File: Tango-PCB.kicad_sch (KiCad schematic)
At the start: 60 parts, among them J1 PMOD, J10 Screw_Terminal_01x03, J11 Screw_Terminal_01x03, J12 Screw_Terminal_01x03, J13 Screw_Terminal_01x03, J14 Screw_Terminal_01x03, J15 Screw_Terminal_01x03, J16 Screw_Terminal_01x03, J17 Screw_Terminal_01x03, J18 Screw_Terminal_01x03, J19 Screw_Terminal_01x03, J2 EXT, J20 Screw_Terminal_01x03, J21 Screw_Terminal_01x03, J22 PWR, J23 SENSPWR, J26 PMOD, J3 Screw_Terminal_01x04, J4 Screw_Terminal_01x04, J5 Screw_Terminal_01x04, J6 Screw_Terminal_01x04, J7 Screw_Terminal_01x04, J8 Screw_Terminal_01x04, J9 Screw_Terminal_01x03, U1 ULN2803A, U2 ULN2803A, U3 ULN2803A

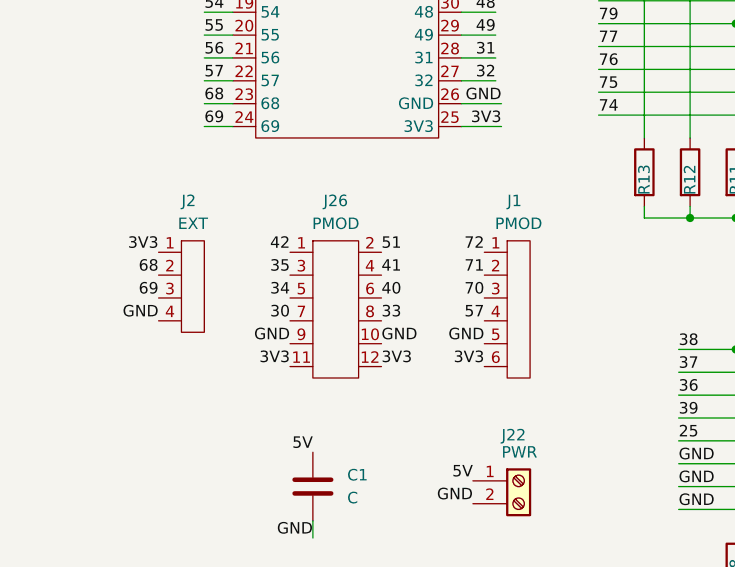
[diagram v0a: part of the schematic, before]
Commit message: Add SPI connector
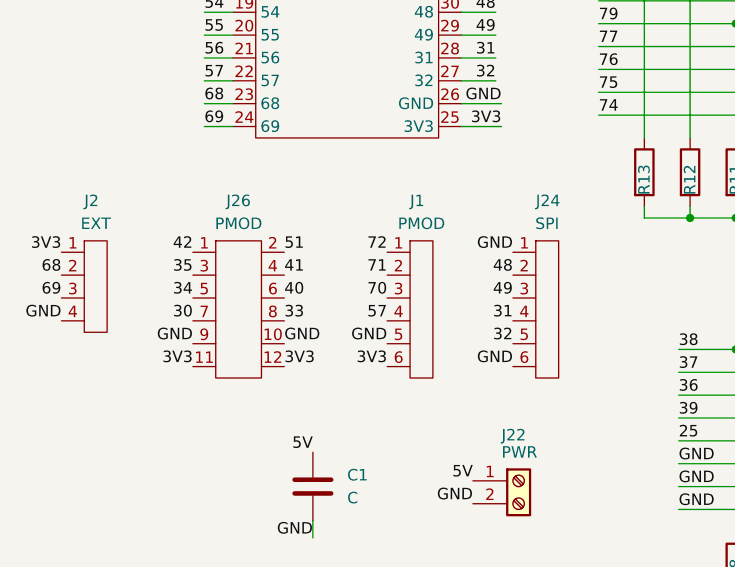
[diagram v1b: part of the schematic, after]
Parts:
- added J24: SPI, Connector_JST:JST_XH_S6B-XH-A-1_1x06_P2.50mm_Horizontal, symbol Library:Conn)01x06_pin
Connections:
- net 31: now also J24.4
- net 32: now also J24.5
- net 48: now also J24.2
- net 49: now also J24.3
- net GND: now also J24.1, J24.6
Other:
- moved on the sheet: J1, J2, J26

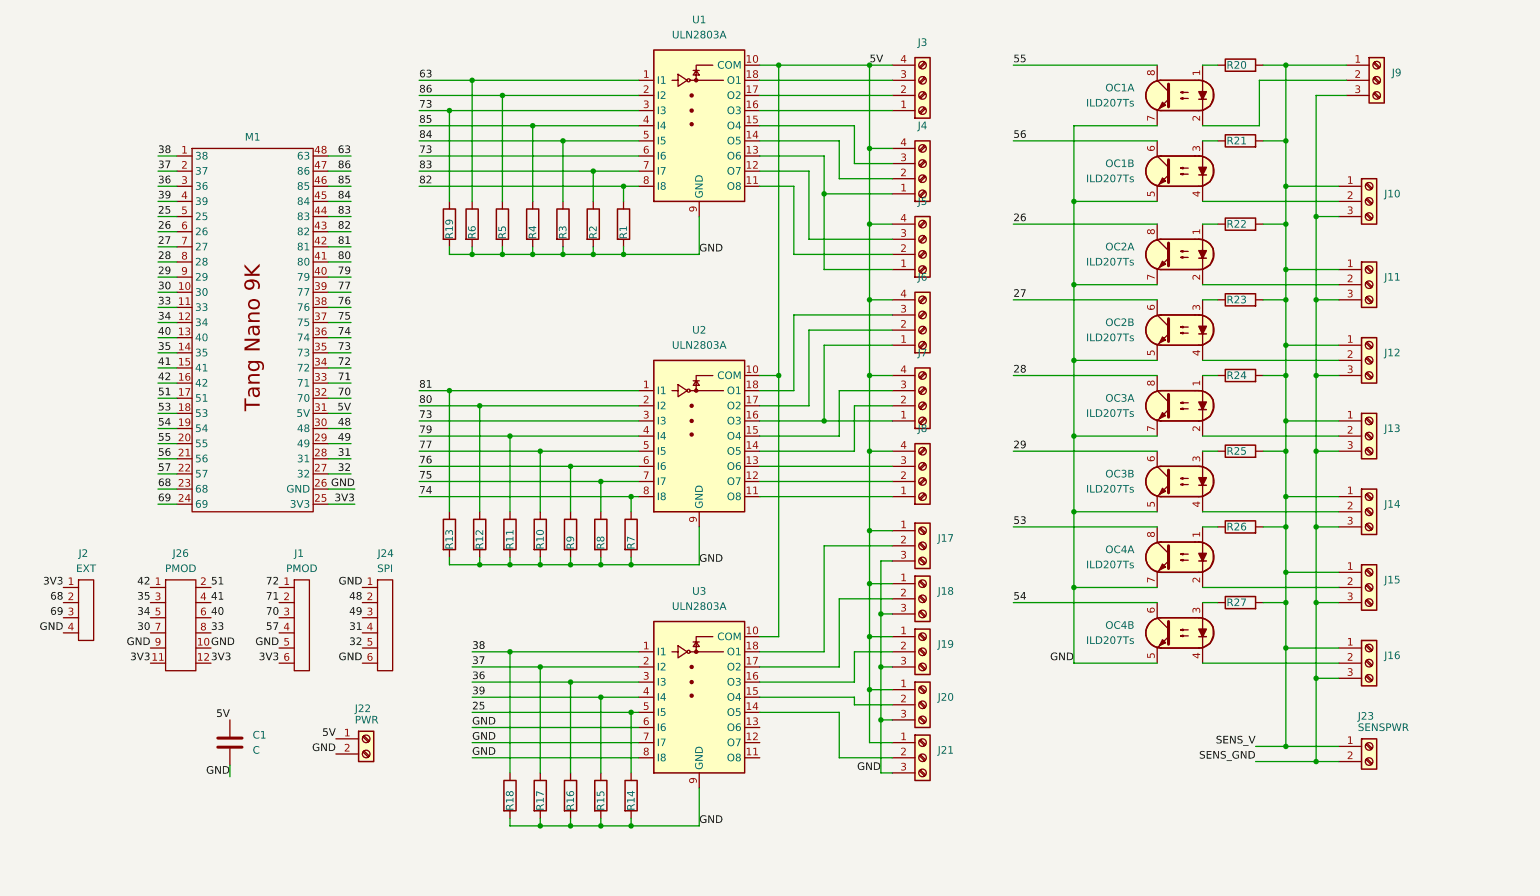
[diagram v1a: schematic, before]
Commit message: V2 - Individually select inputs 5V or 24V. Select input resistor.
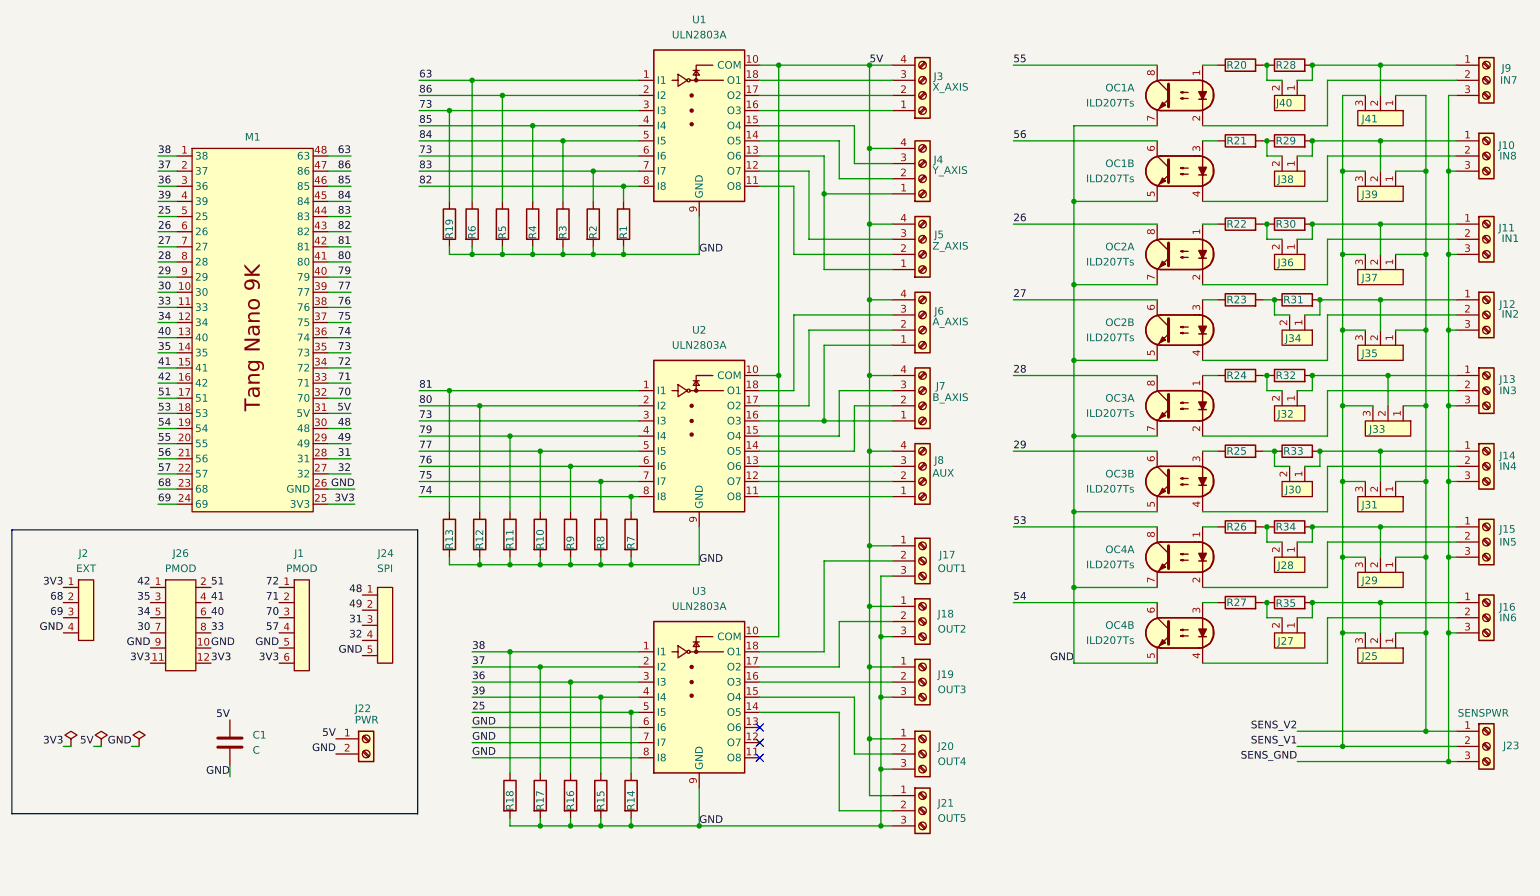
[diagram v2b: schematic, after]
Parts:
- added J25, J29, J31, J33, J35, J37, J39, J41: Sense Power Select, Connector_PinHeader_2.54mm:PinHeader_1x03_P2.54mm_Vertical, symbol Library:Conn_01X03_pin
- added J27, J28, J30, J32, J34, J36, J38, J40: Led resistor select, Connector_PinHeader_2.54mm:PinHeader_1x02_P2.54mm_Vertical, symbol Library:Conn_01X02_pin
- added R28, R29, R30, R31, R32, R33, R34, R35: R, Resistor_SMD:R_0805_2012Metric, symbol Device:R
- J1: symbol Library:Conn)01x06_pin -> Library:Conn_01x06_pin
- J10: value Screw_Terminal_01x03 -> IN8
- J11: value Screw_Terminal_01x03 -> IN1
- J12: value Screw_Terminal_01x03 -> IN2
- J13: value Screw_Terminal_01x03 -> IN3
- J14: value Screw_Terminal_01x03 -> IN4
- J15: value Screw_Terminal_01x03 -> IN5
- J16: value Screw_Terminal_01x03 -> IN6
- J17: value Screw_Terminal_01x03 -> OUT1
- J18: value Screw_Terminal_01x03 -> OUT2
- J19: value Screw_Terminal_01x03 -> OUT3
- J20: value Screw_Terminal_01x03 -> OUT4
- J21: value Screw_Terminal_01x03 -> OUT5
- J23: footprint TerminalBlock_Phoenix:TerminalBlock_Phoenix_PT-1,5-2-3.5-H_1x02_P3.50mm_Horizontal -> TerminalBlock_Phoenix:TerminalBlock_Phoenix_PT-1,5-3-3.5-H_1x03_P3.50mm_Horizontal; symbol Connector:Screw_Terminal_01x02 -> Connector:Screw_Terminal_01x03
- J24: footprint Connector_JST:JST_XH_S6B-XH-A-1_1x06_P2.50mm_Horizontal -> Connector_JST:JST_XH_S5B-XH-A_1x05_P2.50mm_Horizontal; symbol Library:Conn)01x06_pin -> Library:Conn_01x05_pin
- J3: value Screw_Terminal_01x04 -> X_AXIS
- J4: value Screw_Terminal_01x04 -> Y_AXIS
- J5: value Screw_Terminal_01x04 -> Z_AXIS
- J6: value Screw_Terminal_01x04 -> A_AXIS
- J7: value Screw_Terminal_01x04 -> B_AXIS
- J8: value Screw_Terminal_01x04 -> AUX
- J9: value Screw_Terminal_01x03 -> IN7
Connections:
- net 31: now also J24.3; no longer J24.4
- net 32: now also J24.4; no longer J24.5
- net 48: now also J24.1; no longer J24.2
- net 49: now also J24.2; no longer J24.3
- net GND: now also J24.5; no longer J24.1, J24.6
- net SENS_GND: now also J23.3 (Pin_3); no longer J23.2 (Pin_2)
- removed net SENS_V: J10.1 (Pin_1), J11.1 (Pin_1), J12.1 (Pin_1), J13.1 (Pin_1), J14.1 (Pin_1), J15.1 (Pin_1), J16.1 (Pin_1), J23.1 (Pin_1), J9.1 (Pin_1), R20.2, R21.2, R22.2, R23.2, R24.2, R25.2, R26.2, R27.2
- new net: J14.1 (Pin_1), J30.1, J31.2, R33.2
- new net: J30.2, R25.2, R33.1
- new net: J13.1 (Pin_1), J32.1, J33.2, R32.2
- new net: J27.2, R27.2, R35.1
- new net: J11.1 (Pin_1), J36.1, J37.2, R30.2
- new net: J36.2, R22.2, R30.1
- new net: J12.1 (Pin_1), J34.1, J35.2, R31.2
- new net: J10.1 (Pin_1), J38.1, J39.2, R29.2
- new net: J15.1 (Pin_1), J28.1, J29.2, R34.2
- new net: J28.2, R26.2, R34.1
- new net: J32.2, R24.2, R32.1
- new net: J40.1, J41.2, J9.1 (Pin_1), R28.2
- new net: J40.2, R20.2, R28.1
- new net: J16.1 (Pin_1), J25.2, J27.1, R35.2
- new net: J38.2, R21.2, R29.1
- new net: J34.2, R23.2, R31.1
- new net SENS_V1: J23.2 (Pin_2), J25.3, J29.3, J31.3, J33.3, J35.3, J37.3, J39.3, J41.3
- new net SENS_V2: J23.1 (Pin_1), J25.1, J29.1, J31.1, J33.1, J35.1, J37.1, J39.1, J41.1
- no-connect marks 0 -> 3
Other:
- moved on the sheet: J10, J11, J12, J13, J14, J15, J16, J17, J18, J19, J20, J21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

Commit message: Updates.
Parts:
- added C2, C3, C4: 100n, Capacitor_SMD:C_0805_2012Metric, symbol Device:C
- C1: value C -> 100n
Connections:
- net 3V3: now also C2.1, C3.1, C4.1
- net GND: now also C2.2, C3.2, C4.2
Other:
- moved on the sheet: C1, J1, J17, J18, J19, J20, J21, J22, J24, J26, J3, J4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

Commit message: Update.
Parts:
- removed R3: R, Resistor_SMD:R_0805_2012Metric, symbol Device:R
- added H1, H2, H3, H4: MountingHole, MountingHole:MountingHole_3.2mm_M3_Pad, symbol Mechanical:MountingHole
- added R1: R, Resistor_SMD:R_0805_2012Metric, symbol Device:R
- renumbered J22 to J1, J6 to J10, J7 to J11, J8 to J12, J17 to J13, J18 to J14, J19 to J15, J20 to J16, J21 to J17, J9 to J18, J10 to J19, J23 to J2, J11 to J20, J12 to J21, J13 to J22, J14 to J23, J15 to J24, J16 to J25, J40 to J26, J41 to J27, J38 to J28, J39 to J29, J2 to J3, J36 to J30, J37 to J31, J34 to J32, J35 to J33, J32 to J34, J33 to J35, J30 to J36, J31 to J37, J28 to J38, J29 to J39, J26 to J4, J27 to J40, J25 to J41, J1 to J5, J24 to J6, J3 to J7, J4 to J8, J5 to J9, R11 to R10, R10 to R11, R9 to R12, R8 to R13, R7 to R14, R18 to R15, R17 to R16, R16 to R17, R15 to R18, R14 to R19, R19 to R2, R28 to R21, R21 to R22, R29 to R23, R22 to R24, R30 to R25, R23 to R26, R31 to R27, R24 to R28, R32 to R29, R6 to R3, R25 to R30, R33 to R31, R26 to R32, R34 to R33, R27 to R34, R5 to R4, R4 to R5, R2 to R6, R1 to R7, R13 to R8, R12 to R9
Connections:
- net 63: now also R1.1; no longer R3.1
- net 73: now also R3.1; no longer R2.1
- net 84: now also R5.1
- net 85: now also R4.1; no longer R5.1
- net 86: now also R2.1; no longer R4.1
- net GND: now also R1.2
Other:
- moved on the sheet: J32, J35, J36, R10, R11, R12, R13, R15, R16, R17, R18, R2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
